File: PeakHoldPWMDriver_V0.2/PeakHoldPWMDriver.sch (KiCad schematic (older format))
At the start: 77 parts, among them J1 Screw_Terminal_01x06, J2 Screw_Terminal_01x08, Q1 AO3400, Q10 AO3401A, Q11 AO3401A, Q12 BSP78, Q14 BSP78, Q17 AO3422, Q19 AO3422, Q2 AO3400, Q20 AO3401A, Q21 BSP78, Q22 AO3401A, Q23 BSP78, Q3 AO3400, Q4 AO3400, Q8 AO3422, Q9 AO3422, U10 74LS08, U11 74LS08, U2 LM78M05_TO220, U4 74LS32, U6 LM2901, U7 LTC6992, U8 74LS74, U9 74LS74

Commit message: Routing board V0.2
Work done on new PCB
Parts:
- removed D2: BLUE, LED_SMD:LED_0603_1608Metric_Pad1.05x0.95mm_HandSolder, symbol Device:LED
- removed D3: D_Zener_Small, Diode_SMD:D_MiniMELF_Handsoldering, symbol Device:D_Zener_Small
- removed D4: 40V-1A, Diode_SMD:D_SMA-SMB_Universal_Handsoldering, symbol Speeduino_base-eagle-import:SMD-DIODE-SCHOTTKY-40V-1A(DO-214AC)
- removed R75: 560, Resistor_SMD:R_0603_1608Metric_Pad1.05x0.95mm_HandSolder, symbol Speeduino_base-eagle-import:SMD-RES-470R-5%-1_10W(0603)
- added C1, C2, C3: SVPF 1,0M 16, Capacitor_SMD:CP_Elec_10x12.5, symbol Device:CP_Small
- added C10: 220nf, Capacitor_SMD:C_0603_1608Metric_Pad1.05x0.95mm_HandSolder, symbol Speeduino_base-eagle-import:CERAMIC-220NF-25V-10%-X7R(0603)
- added D3: 1N4007, Diode_SMD:D_SMA, symbol Device:D_Schottky_Small
- added H1, H2, H3, H4: MountingHole_Pad, MountingHole:MountingHole_2.5mm_Pad, symbol Mechanical:MountingHole_Pad
- added R8: 8K2, Resistor_SMD:R_0603_1608Metric_Pad1.05x0.95mm_HandSolder, symbol Device:R_Small
- added TP1: PeakTP, TestPoint:TestPoint_Pad_1.0x1.0mm, symbol Connector:TestPoint
- added TP2: HoldTP, TestPoint:TestPoint_Pad_1.0x1.0mm, symbol Connector:TestPoint
- D1: renamed from D18; value LL4148 -> BAV103
- D4: renamed from D22; value LL4148 -> BAV103
- D6: renamed from D31; value SS310 -> 1N4007; footprint Diode_SMD:D_SMA-SMB_Universal_Handsoldering -> Diode_SMD:D_SMA
- D7: renamed from D32; value SS310 -> 1N4007; footprint Diode_SMD:D_SMA-SMB_Universal_Handsoldering -> Diode_SMD:D_SMA
- D8: renamed from D34; value SS310 -> 1N4007; footprint Diode_SMD:D_SMA-SMB_Universal_Handsoldering -> Diode_SMD:D_SMA
- D9: renamed from D35; value SS310 -> 1N4007; footprint Diode_SMD:D_SMA-SMB_Universal_Handsoldering -> Diode_SMD:D_SMA
- J1: footprint Connector_Phoenix_MSTB:PhoenixContact_MSTBV_2,5_6-GF-5,08_1x06_P5.08mm_Vertical_ThreadedFlange -> Connector_Phoenix_MSTB:PhoenixContact_MSTBA_2,5_6-G-5,08_1x06_P5.08mm_Horizontal
- J2: footprint Connector_Phoenix_MSTB:PhoenixContact_MSTBV_2,5_8-GF-5,08_1x08_P5.08mm_Vertical_ThreadedFlange -> Connector_Phoenix_MSTB:PhoenixContact_MSTBA_2,5_8-G-5,08_1x08_P5.08mm_Horizontal
- Q11: renamed from Q17; value AO3422 -> 2N7002
- Q12: renamed from Q19; value AO3422 -> 2N7002
- Q13: renamed from Q20; value AO3401A -> TSM2309
- Q15: renamed from Q22; value AO3401A -> TSM2309
- Q3: renamed from Q8; value AO3422 -> 2N7002
- Q4: renamed from Q9; value AO3422 -> 2N7002
- Q5: renamed from Q10; value AO3401A -> TSM2309
- Q6: renamed from Q11; value AO3401A -> TSM2309
- U6: renamed from U2; footprint Package_TO_SOT_THT:TO-220-3_Vertical -> Package_TO_SOT_SMD:SOT-223-3_TabPin2
- renumbered C6 to C5, C23 to C6, C8 to C7, C14 to C8, C16 to C9, D20 to D2, D1 to D5, F2 to F1, F1 to F2, Q4 to Q10, Q21 to Q14, Q23 to Q16, Q12 to Q7, Q14 to Q8, Q3 to Q9, R2 to R1, R77 to R10, R78 to R11, R79 to R12, R80 to R13, R84 to R14, R85 to R15, R88 to R16, R89 to R17, R90 to R18, R91 to R19, R53 to R2, R4 to R20, R5 to R21, R96 to R22, R97 to R23, R98 to R24, R99 to R25, R100 to R26, R102 to R27, R105 to R28, R108 to R29, R56 to R3, R109 to R30, R111 to R31, R58 to R4, R73 to R5, R65 to R6, R1 to R7, R3 to R9, U4 to U1, U6 to U2, U8 to U3, U7 to U4, U9 to U5, U10 to U7, U11 to U8
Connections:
- net INJ1: now also J1.4 (Pin_4); no longer J1.3 (Pin_3)
- net INJ2: now also J1.3 (Pin_3); no longer J1.4 (Pin_4)
- net INJ3: now also J1.2 (Pin_2); no longer J1.5 (Pin_5)
- net INJ4: now also J1.1 (Pin_1); no longer J1.6 (Pin_6)
- net PWM: now also R8.2
- net PWR_GND: now also J1.5 (Pin_5), C1.2, C10.2, C2.2, C3.2, H1.1, H2.1, H3.1, H4.1; no longer J1.2 (Pin_2)
- net VBAT: now also C1.1, C2.1, C3.1
- net VBAT_IN: now also J1.6 (Pin_6); no longer J1.1 (Pin_1)
- net VREF: now also U2.11 (+), U2.5 (+), U2.7 (+), U2.9 (+), TP1.1; no longer U2.10 (-), U2.4 (-), U2.6 (-), U2.8 (-)
- net inv_INJ1: now also U8.13; no longer U7.5
- net inv_INJ4: now also U7.5; no longer U8.13
- net at C5.2, C7.2, U6.1 (VI): now also D3.1 (K)
- net at F2.2: now also D3.2 (A)
- net at Q7.3 (S), R16.1: now also U2.4 (-); no longer U2.5 (+)
- net at Q8.3 (S), R17.1: now also U2.8 (-); no longer U2.11 (+)
- net at Q16.3 (S), R30.1: now also U2.10 (-); no longer U2.9 (+)
- net at Q14.3 (S), R28.1: now also U2.6 (-); no longer U2.7 (+)
- net at R19.2, U5.4 (~S): now also U2.14; no longer U2.13
- net at R31.2, U5.10 (~S): now also U2.13; no longer U2.14
- net at U3.6 (~Q): now also U8.12; no longer U7.4
- net at U7.6: now also U1.13; no longer U1.2
- net at U8.11: now also U1.2; no longer U1.13
- net at U5.8 (~Q): now also U7.4; no longer U8.12
- new net: C10.1, R8.1, TP2.1
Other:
- moved on the sheet: U7B, U8D

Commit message: routed V0.2
New board fully routed
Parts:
- D6, D7, D8, D9: value 1N4007 -> SS33
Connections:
- net inv_INJ1: now also U8.10; no longer U7.2
- net inv_INJ4: now also U7.2; no longer U8.10
- net at Q8.3 (S), R17.1: now also U2.10 (-); no longer U2.8 (-)
- net at Q16.3 (S), R30.1: now also U2.8 (-); no longer U2.10 (-)
- net at R19.2, U5.4 (~S): now also U2.13; no longer U2.14
- net at R31.2, U5.10 (~S): now also U2.14; no longer U2.13
- net at U1.1: now also U8.8; no longer U7.3
- net at U1.12: now also U7.3; no longer U8.8
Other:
- moved on the sheet: U2C, U2D, U7A, U8C
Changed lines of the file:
@@
 P 10250 3800
 F 0 "D9" H 10250 3687 50  0000 C CNN
-F 1 "1N4007" V 10295 3868 50  0001 L CNN
+F 1 "SS33" V 10295 3868 50  0001 L CNN
 F 2 "Diode_SMD:D_SMA" V 10250 3800 50  0001 C CNN
 F 3 "~" V 10250 3800 50  0001 C CNN
@@
 P 9950 900
 F 0 "D8" H 9950 787 50  0000 C CNN
-F 1 "1N4007" V 9995 968 50  0001 L CNN
+F 1 "SS33" V 9995 968 50  0001 L CNN
 F 2 "Diode_SMD:D_SMA" V 9950 900 50  0001 C CNN
 F 3 "~" V 9950 900 50  0001 C CNN
@@
 P 7350 3700
 F 0 "D7" H 7350 3587 50  0000 C CNN
-F 1 "1N4007" V 7395 3768 50  0001 L CNN
+F 1 "SS33" V 7395 3768 50  0001 L CNN
 F 2 "Diode_SMD:D_SMA" V 7350 3700 50  0001 C CNN
 F 3 "~" V 7350 3700 50  0001 C CNN
@@
 L Comparator:LM2901 U2
 U 4 1 5EDAB68D
-P 7800 5150
-F 0 "U2" H 7800 5517 50  0000 C CNN
-F 1 "LM2901" H 7800 5426 50  0000 C CNN
-F 2 "Package_SO:SO-14_5.3x10.2mm_P1.27mm" H 7750 5250 50  0001 C CNN
-F 3 "https://www.st.com/resource/en/datasheet/lm2901.pdf" H 7850 5350 50  0001 C CNN
-	4    7800 5150
+P 10750 5250
+F 0 "U2" H 10750 5617 50  0000 C CNN
+F 1 "LM2901" H 10750 5526 50  0000 C CNN
+F 2 "Package_SO:SO-14_5.3x10.2mm_P1.27mm" H 10700 5350 50  0001 C CNN
+F 3 "https://www.st.com/resource/en/datasheet/lm2901.pdf" H 10800 5450 50  0001 C CNN
+	4    10750 5250
 	0    1    1    0
 $EndComp
@@
 L Comparator:LM2901 U2
 U 3 1 5EDAC925
-P 10750 5250
-F 0 "U2" H 10750 5617 50  0000 C CNN
-F 1 "LM2901" H 10750 5526 50  0000 C CNN
-F 2 "Package_SO:SO-14_5.3x10.2mm_P1.27mm" H 10700 5350 50  0001 C CNN
-F 3 "https://www.st.com/resource/en/datasheet/lm2901.pdf" H 10800 5450 50  0001 C CNN
-	3    10750 5250
+P 7800 5150
+F 0 "U2" H 7800 5517 50  0000 C CNN
+F 1 "LM2901" H 7800 5426 50  0000 C CNN
+F 2 "Package_SO:SO-14_5.3x10.2mm_P1.27mm" H 7750 5250 50  0001 C CNN
+F 3 "https://www.st.com/resource/en/datasheet/lm2901.pdf" H 7850 5350 50  0001 C CNN
+	3    7800 5150
 	0    1    1    0
 $EndComp
@@
 L 74xx:74LS08 U7
 U 1 1 5F61AD4C
-P 5750 2600
-F 0 "U7" H 5750 2283 50  0000 C CNN
-F 1 "74LS08" H 5750 2374 50  0000 C CNN
-F 2 "Package_SO:SO-14_5.3x10.2mm_P1.27mm" H 5750 2600 50  0001 C CNN
-F 3 "http://www.ti.com/lit/gpn/sn74LS08" H 5750 2600 50  0001 C CNN
-	1    5750 2600
+P 8850 5450
+F 0 "U7" H 8850 5133 50  0000 C CNN
+F 1 "74LS08" H 8850 5224 50  0000 C CNN
+F 2 "Package_SO:SO-14_5.3x10.2mm_P1.27mm" H 8850 5450 50  0001 C CNN
+F 3 "http://www.ti.com/lit/gpn/sn74LS08" H 8850 5450 50  0001 C CNN
+	1    8850 5450
 	0    1    1    0
 $EndComp
@@
 L 74xx:74LS08 U8
 U 3 1 5F918EE3
-P 8850 5450
-F 0 "U8" H 8850 5133 50  0000 C CNN
-F 1 "74LS08" H 8850 5224 50  0000 C CNN
-F 2 "Package_SO:SO-14_5.3x10.2mm_P1.27mm" H 8850 5450 50  0001 C CNN
-F 3 "http://www.ti.com/lit/gpn/sn74LS08" H 8850 5450 50  0001 C CNN
-	3    8850 5450
+P 5750 2600
+F 0 "U8" H 5750 2283 50  0000 C CNN
+F 1 "74LS08" H 5750 2374 50  0000 C CNN
+F 2 "Package_SO:SO-14_5.3x10.2mm_P1.27mm" H 5750 2600 50  0001 C CNN
+F 3 "http://www.ti.com/lit/gpn/sn74LS08" H 5750 2600 50  0001 C CNN
+	3    5750 2600
 	0    1    1    0
 $EndComp
@@
 P 7300 900
 F 0 "D6" H 7300 787 50  0000 C CNN
-F 1 "1N4007" V 7345 968 50  0001 L CNN
+F 1 "SS33" V 7345 968 50  0001 L CNN
 F 2 "Diode_SMD:D_SMA" V 7300 900 50  0001 C CNN
 F 3 "~" V 7300 900 50  0001 C CNN

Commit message: Cleanup of board
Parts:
- C1, C2, C3: value SVPF 1,0M 16 -> 1mF
- D2: value SS310 -> BAV103
- D6, D7, D8, D9: value SS33 -> SS36
- R14, R15, R2, R26, R27, R6: value 470 -> 470R
- R5: value 180 -> 180R
- R8: value 8K2 -> 10k
- U6: value LM78M05_TO220 -> LM78M05
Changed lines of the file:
@@
 P 3300 950
 F 0 "R5" H 3150 1000 42  0000 L BNN
-F 1 "180" H 3150 850 42  0000 L BNN
+F 1 "180R" H 3150 850 42  0000 L BNN
 F 2 "Resistor_SMD:R_0603_1608Metric_Pad1.05x0.95mm_HandSolder" H 3300 950 50  0001 C CNN
 F 3 "" H 3300 950 50  0001 C CNN
@@
 P 3100 3000
 F 0 "U6" H 3100 3242 50  0000 C CNN
-F 1 "LM78M05_TO220" H 3100 3151 50  0000 C CNN
+F 1 "LM78M05" H 3100 3151 50  0000 C CNN
 F 2 "Package_TO_SOT_SMD:SOT-223-3_TabPin2" H 3100 3225 50  0001 C CIN
 F 3 "http://www.fairchildsemi.com/ds/LM/LM78M05.pdf" H 3100 2950 50  0001 C CNN
@@
 P 10250 3800
 F 0 "D9" H 10250 3687 50  0000 C CNN
-F 1 "SS33" V 10295 3868 50  0001 L CNN
+F 1 "SS36" V 10295 3868 50  0001 L CNN
 F 2 "Diode_SMD:D_SMA" V 10250 3800 50  0001 C CNN
 F 3 "~" V 10250 3800 50  0001 C CNN
@@
 P 9600 4100
 F 0 "R27" H 9659 4146 50  0000 L CNN
-F 1 "470" H 9659 4055 50  0000 L CNN
+F 1 "470R" H 9659 4055 50  0000 L CNN
 F 2 "Resistor_SMD:R_0603_1608Metric_Pad1.05x0.95mm_HandSolder" H 9600 4100 50  0001 C CNN
 F 3 "~" H 9600 4100 50  0001 C CNN
@@
 P 9950 900
 F 0 "D8" H 9950 787 50  0000 C CNN
-F 1 "SS33" V 9995 968 50  0001 L CNN
+F 1 "SS36" V 9995 968 50  0001 L CNN
 F 2 "Diode_SMD:D_SMA" V 9950 900 50  0001 C CNN
 F 3 "~" V 9950 900 50  0001 C CNN
@@
 P 9450 1200
 F 0 "R26" H 9509 1246 50  0000 L CNN
-F 1 "470" H 9509 1155 50  0000 L CNN
+F 1 "470R" H 9509 1155 50  0000 L CNN
 F 2 "Resistor_SMD:R_0603_1608Metric_Pad1.05x0.95mm_HandSolder" H 9450 1200 50  0001 C CNN
 F 3 "~" H 9450 1200 50  0001 C CNN
@@
 P 7350 3700
 F 0 "D7" H 7350 3587 50  0000 C CNN
-F 1 "SS33" V 7395 3768 50  0001 L CNN
+F 1 "SS36" V 7395 3768 50  0001 L CNN
 F 2 "Diode_SMD:D_SMA" V 7350 3700 50  0001 C CNN
 F 3 "~" V 7350 3700 50  0001 C CNN
@@
 P 6750 4000
 F 0 "R15" H 6809 4046 50  0000 L CNN
-F 1 "470" H 6809 3955 50  0000 L CNN
+F 1 "470R" H 6809 3955 50  0000 L CNN
 F 2 "Resistor_SMD:R_0603_1608Metric_Pad1.05x0.95mm_HandSolder" H 6750 4000 50  0001 C CNN
 F 3 "~" H 6750 4000 50  0001 C CNN
@@
 P 6700 1200
 F 0 "R14" H 6759 1246 50  0000 L CNN
-F 1 "470" H 6759 1155 50  0000 L CNN
+F 1 "470R" H 6759 1155 50  0000 L CNN
 F 2 "Resistor_SMD:R_0603_1608Metric_Pad1.05x0.95mm_HandSolder" H 6700 1200 50  0001 C CNN
 F 3 "~" H 6700 1200 50  0001 C CNN
@@
 P 1350 6300
 F 0 "R2" H 1409 6346 50  0000 L CNN
-F 1 "470" H 1409 6255 50  0000 L CNN
+F 1 "470R" H 1409 6255 50  0000 L CNN
 F 2 "Resistor_SMD:R_0603_1608Metric_Pad1.05x0.95mm_HandSolder" H 1350 6300 50  0001 C CNN
 F 3 "~" H 1350 6300 50  0001 C CNN
@@
 	1550 6700 1700 6700
 $Comp
-L Device:D_Schottky_Small D2
-U 1 1 5F0A32EC
-P 1850 7050
-F 0 "D2" H 1850 6937 50  0000 C CNN
-F 1 "SS310" V 1895 7118 50  0001 L CNN
-F 2 "Diode_SMD:D_MiniMELF" V 1850 7050 50  0001 C CNN
-F 3 "~" V 1850 7050 50  0001 C CNN
-	1    1850 7050
-	0    -1   -1   0
-$EndComp
-$Comp
 L Speeduino_base-eagle-import:SMD-RES-470R-5%-1_10W(0603) R4
 U 1 1 5F0A3829
@@
 P 3450 6500
 F 0 "R6" H 3509 6546 50  0000 L CNN
-F 1 "470" H 3509 6455 50  0000 L CNN
+F 1 "470R" H 3509 6455 50  0000 L CNN
 F 2 "Resistor_SMD:R_0603_1608Metric_Pad1.05x0.95mm_HandSolder" H 3450 6500 50  0001 C CNN
 F 3 "~" H 3450 6500 50  0001 C CNN
@@
 P 2000 1950
 F 0 "C3" H 1912 1904 50  0000 R CNN
-F 1 "SVPF 1,0M 16" H 1912 1995 50  0000 R CNN
+F 1 "1mF" H 1912 1995 50  0000 R CNN
 F 2 "Capacitor_SMD:CP_Elec_10x12.5" H 2000 1950 50  0001 C CNN
 F 3 "~" H 2000 1950 50  0001 C CNN
@@
 P 1700 1950
 F 0 "C2" H 1612 1904 50  0000 R CNN
-F 1 "SVPF 1,0M 16" H 1612 1995 50  0000 R CNN
+F 1 "1mF" H 1612 1995 50  0000 R CNN
 F 2 "Capacitor_SMD:CP_Elec_10x12.5" H 1700 1950 50  0001 C CNN
 F 3 "~" H 1700 1950 50  0001 C CNN
@@
 P 1400 1950
 F 0 "C1" H 1312 1904 50  0000 R CNN
-F 1 "SVPF 1,0M 16" H 1312 1995 50  0000 R CNN
+F 1 "1mF" H 1312 1995 50  0000 R CNN
 F 2 "Capacitor_SMD:CP_Elec_10x12.5" H 1400 1950 50  0001 C CNN
 F 3 "~" H 1400 1950 50  0001 C CNN
@@
 P 5200 6900
 F 0 "R8" H 5259 6946 50  0000 L CNN
-F 1 "8K2" H 5259 6855 50  0000 L CNN
+F 1 "10k" H 5259 6855 50  0000 L CNN
 F 2 "Resistor_SMD:R_0603_1608Metric_Pad1.05x0.95mm_HandSolder" H 5200 6900 50  0001 C CNN
 F 3 "~" H 5200 6900 50  0001 C CNN
@@
 P 7300 900
 F 0 "D6" H 7300 787 50  0000 C CNN
-F 1 "SS33" V 7345 968 50  0001 L CNN
+F 1 "SS36" V 7345 968 50  0001 L CNN
 F 2 "Diode_SMD:D_SMA" V 7300 900 50  0001 C CNN
 F 3 "~" V 7300 900 50  0001 C CNN
@@
 Wire Wire Line
 	2000 2100 2600 2100
+$Comp
+L Device:D_Schottky_Small D2
+U 1 1 5F140CEC
+P 1850 7050
+F 0 "D2" H 1850 6937 50  0000 C CNN
+F 1 "BAV103" V 1895 7118 50  0001 L CNN
+F 2 "Diode_SMD:D_MiniMELF" V 1850 7050 50  0001 C CNN
+F 3 "~" V 1850 7050 50  0001 C CNN
+	1    1850 7050
+	0    -1   -1   0
+$EndComp
 $EndSCHEMATC

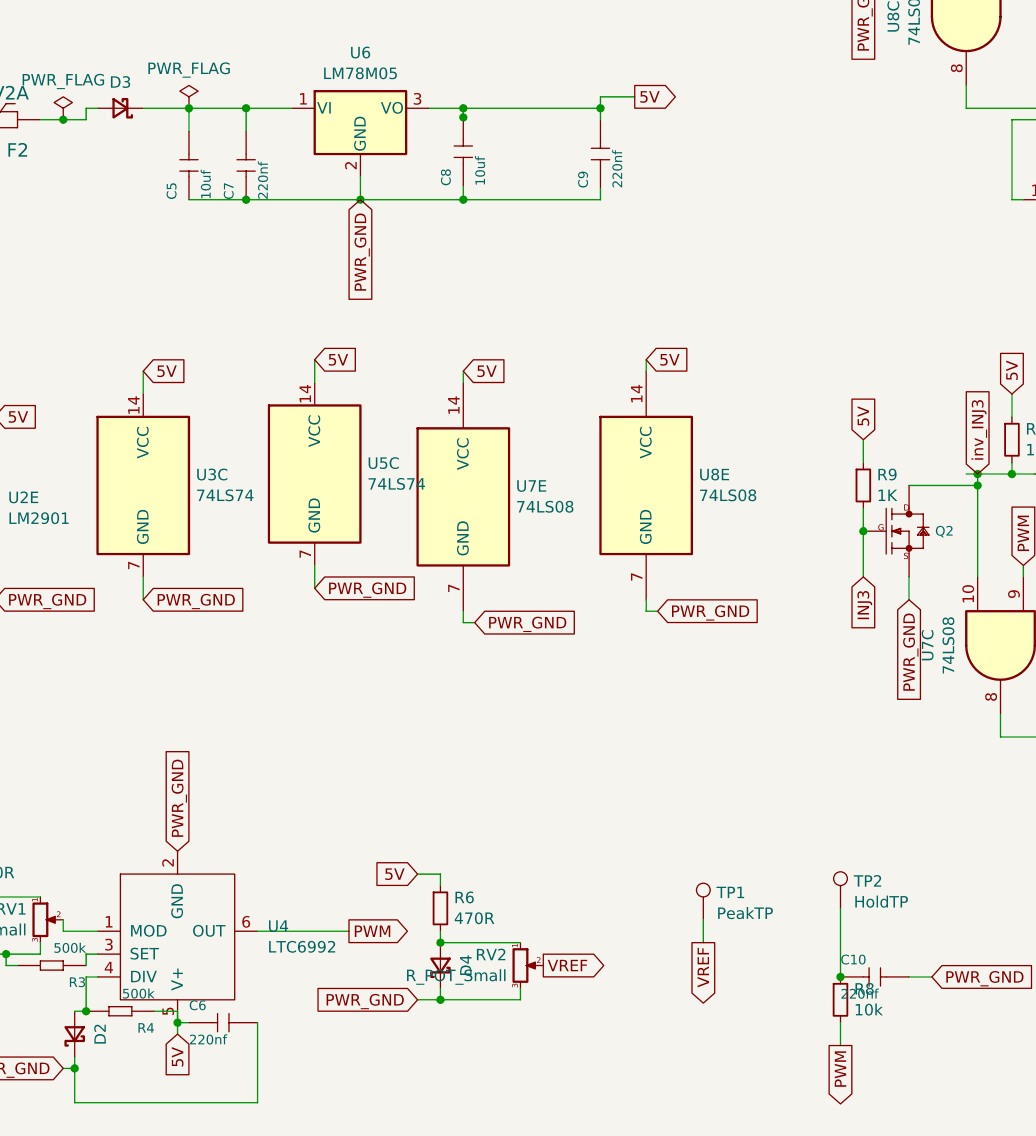
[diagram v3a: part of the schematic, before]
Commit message: renumber all parts
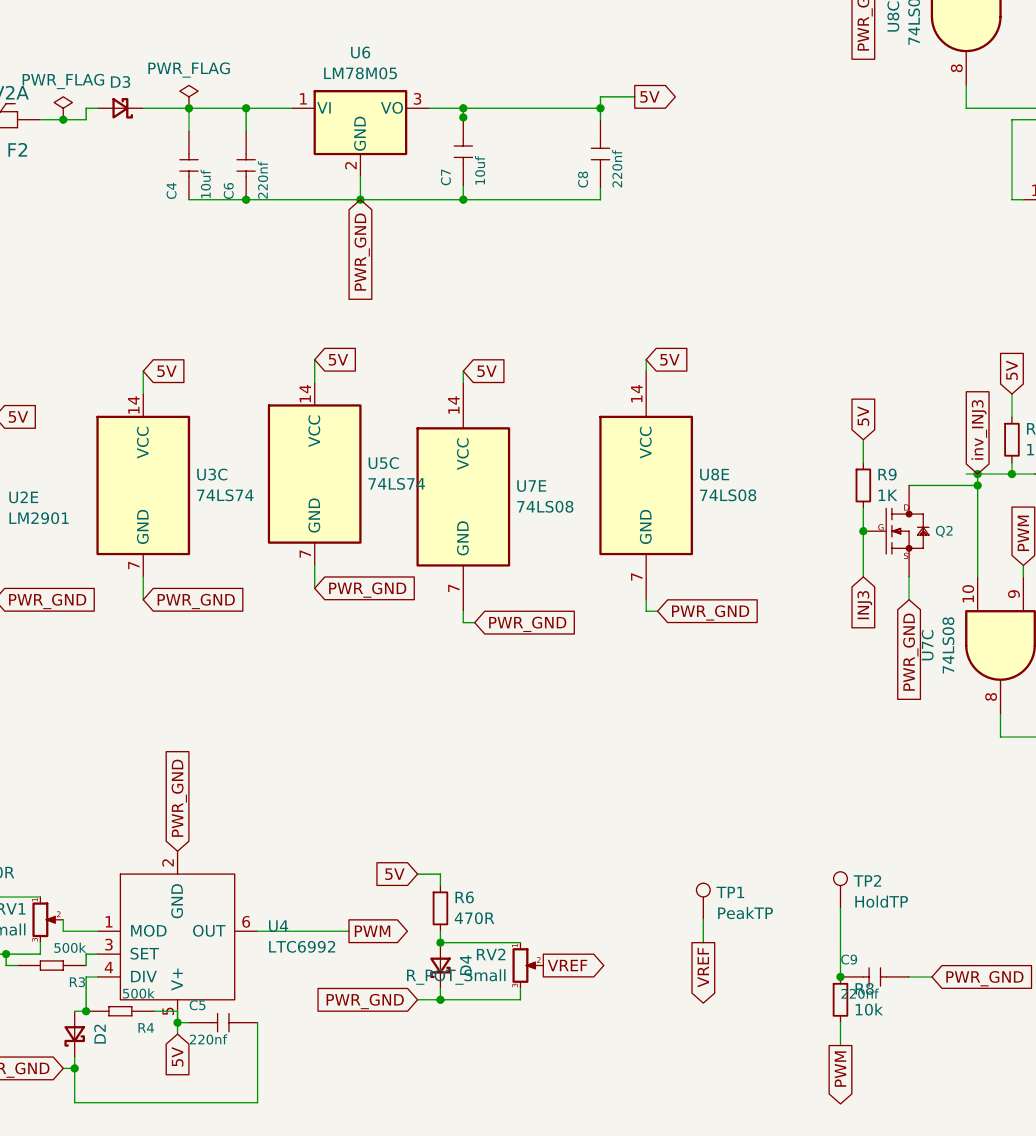
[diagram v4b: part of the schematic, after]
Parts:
- renumbered C5 to C4, C6 to C5, C7 to C6, C8 to C7, C9 to C8, C10 to C9
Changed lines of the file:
@@
 $EndDescr
 $Comp
-L Speeduino_base-eagle-import:CERAMIC-220NF-25V-10%-X7R(0603) C9
+L Speeduino_base-eagle-import:CERAMIC-220NF-25V-10%-X7R(0603) C8
 U 1 1 3AC10700
 P 4150 3200
-F 0 "C9" H 4000 3250 42  0000 L BNN
+F 0 "C8" H 4000 3250 42  0000 L BNN
 F 1 "220nf" H 4000 3100 42  0000 L BNN
 F 2 "Capacitor_SMD:C_0603_1608Metric_Pad1.05x0.95mm_HandSolder" H 4150 3200 50  0001 C CNN
@@
 $EndComp
 $Comp
-L Speeduino_base-eagle-import:CERAMIC-10UF-25V-10%-X5R(1206) C8
+L Speeduino_base-eagle-import:CERAMIC-10UF-25V-10%-X5R(1206) C7
 U 1 1 603F19F2
 P 3550 3190
-F 0 "C8" H 3400 3240 42  0000 L BNN
+F 0 "C7" H 3400 3240 42  0000 L BNN
 F 1 "10uf" H 3400 3090 42  0000 L BNN
 F 2 "Capacitor_SMD:C_1206_3216Metric_Pad1.42x1.75mm_HandSolder" H 3550 3190 50  0001 C CNN
@@
 $EndComp
 $Comp
-L Speeduino_base-eagle-import:CERAMIC-220NF-25V-10%-X7R(0603) C7
+L Speeduino_base-eagle-import:CERAMIC-220NF-25V-10%-X7R(0603) C6
 U 1 1 6187B1B6
 P 2600 3250
-F 0 "C7" H 2450 3300 42  0000 L BNN
+F 0 "C6" H 2450 3300 42  0000 L BNN
 F 1 "220nf" H 2450 3150 42  0000 L BNN
 F 2 "Capacitor_SMD:C_0603_1608Metric_Pad1.05x0.95mm_HandSolder" H 2600 3250 50  0001 C CNN
@@
 PWR_GND
 $Comp
-L Speeduino_base-eagle-import:CERAMIC-10UF-25V-10%-X5R(1206) C5
+L Speeduino_base-eagle-import:CERAMIC-10UF-25V-10%-X5R(1206) C4
 U 1 1 20CCEB9A
 P 2350 3250
-F 0 "C5" H 2200 3300 42  0000 L BNN
+F 0 "C4" H 2200 3300 42  0000 L BNN
 F 1 "10uf" H 2200 3150 42  0000 L BNN
 F 2 "Capacitor_SMD:C_1206_3216Metric_Pad1.42x1.75mm_HandSolder" H 2350 3250 50  0001 C CNN
@@
 	7700 5800 7550 5800
 $Comp
-L Speeduino_base-eagle-import:CERAMIC-220NF-25V-10%-X7R(0603) C6
+L Speeduino_base-eagle-import:CERAMIC-220NF-25V-10%-X7R(0603) C5
 U 1 1 5F4D9CF0
 P 2500 7000
-F 0 "C6" H 2350 7050 42  0000 L BNN
+F 0 "C5" H 2350 7050 42  0000 L BNN
 F 1 "220nf" H 2350 6900 42  0000 L BNN
 F 2 "Capacitor_SMD:C_0603_1608Metric_Pad1.05x0.95mm_HandSolder" H 2500 7000 50  0001 C CNN
@@
 $EndComp
 $Comp
-L Speeduino_base-eagle-import:CERAMIC-220NF-25V-10%-X7R(0603) C10
+L Speeduino_base-eagle-import:CERAMIC-220NF-25V-10%-X7R(0603) C9
 U 1 1 5F2FE71A
 P 5350 6800
-F 0 "C10" H 5200 6850 42  0000 L BNN
+F 0 "C9" H 5200 6850 42  0000 L BNN
 F 1 "220nf" H 5200 6700 42  0000 L BNN
 F 2 "Capacitor_SMD:C_0603_1608Metric_Pad1.05x0.95mm_HandSolder" H 5350 6800 50  0001 C CNN
